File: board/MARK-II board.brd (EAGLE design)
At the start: 130 x 80 mm, 169 parts, among them IC1 MAX3243CPWR, IC10 IFX1963TBV, IC11 IFX1963TBV, IC12 ATTINY441-SSU, IC13 LD1117S33, IC2 FT230XS, IC3 ENC28J60SS, IC4 PCM5100, IC5 IS42S83200, IC6 MCP7940NSN, IC7 FM24CL16BG, IC8 AT25DN256SS, IC9 10M25SAE144, Q1 25MHz, Q2 32.768kHz, Q3 CMI-1275C-050, Q4 25MHz, Q5 18,432MHz, Q6 22.5792MHz, T1 BC337-16 A1, X1 MINI-USBUX60A-MB-5ST, X10 T821-106A1S100, X11 T821-110A1S100, X12 PJ-002BH-SMT-TR, X13 T821-106A1S100, X2 L717SDE09P1ACH4F, X3 L77HDE15SD1CH4R, X4 MD-60SM, X5 RB1-125BAG1A, X6 SJ1-3535NG, X7 MICROSD-HRS_DM3D, X8 BAT-HLD-002-SMT, X9 T821-120A1S100

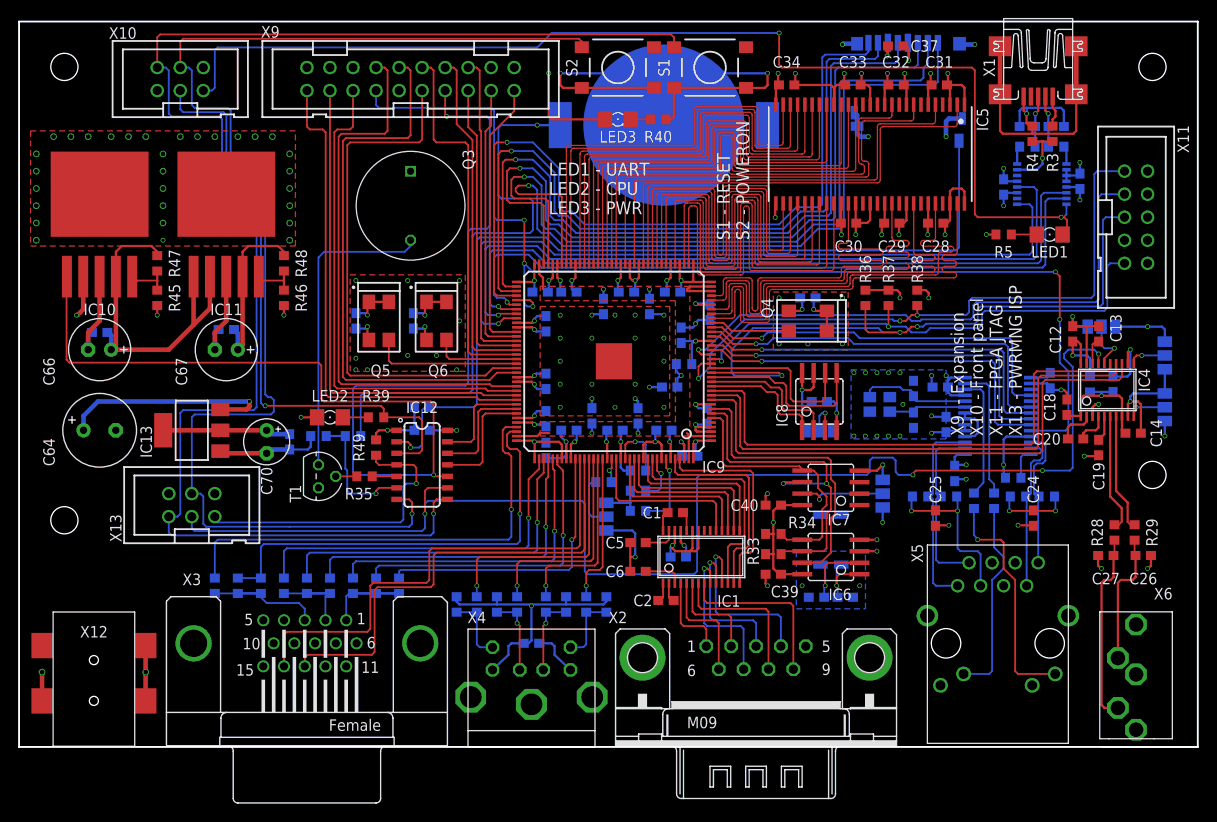
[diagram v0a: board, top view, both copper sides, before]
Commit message: power mng IC changet to Atmega48PB
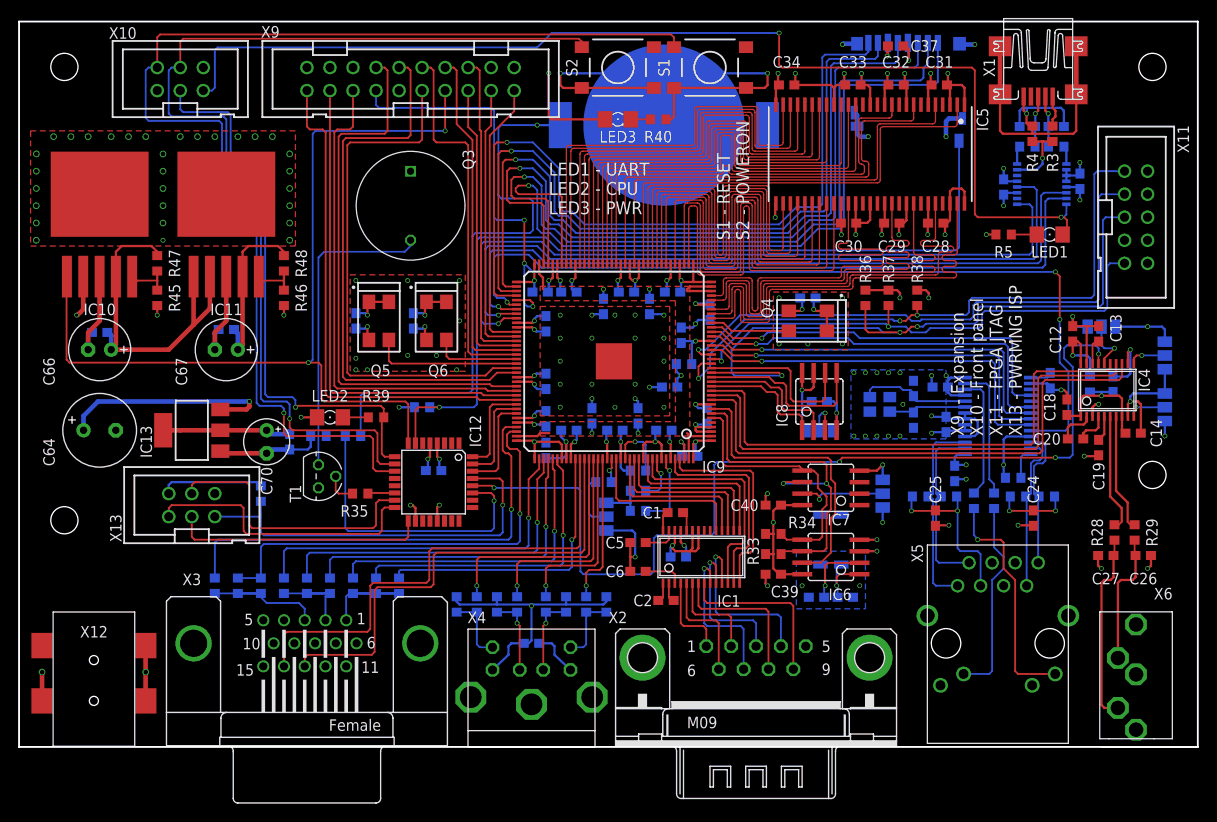
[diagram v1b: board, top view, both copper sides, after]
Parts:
- IC12: value ATTINY441-SSU -> ATMEGA48PB-AU; device ic:SO14 -> ic:TQFP32-08
- moved R49 13.7 mm to (26.7, 27.9), flipped to the bottom
- moved C65 4.62 mm to (45.7, 30.5), turned to 0 degrees
- moved IC12 2.84 mm to (45.7, 29.2)
- moved R35 1.96 mm to (37.6, 27.9)
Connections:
- removed net AUDIO_MUTE/ISP_SCK: IC12.9, IC4.17, X13.3
- removed net POWER_BTN/ISP_MOSI: IC12.7, S2.1, X10.4, X13.4
- removed net RESET_BTN/ISP_MISO: IC12.8, S1.1, X10.2, X13.1
- new net AUDIO_MUTE: IC12.28, IC4.17
- new net ISP_MISO: IC12.16, X13.1
- new net ISP_MOSI: IC12.15, X13.4
- new net ISP_SCK: IC12.17, X13.3
- new net POWER_BTN: IC12.10, S2.1, X10.4
- new net RESET_BTN: IC12.11, S1.1, X10.2
- net +3V3_SB: now also IC12.18, IC12.4; no longer IC12.1
- net CPU_LED: now also IC12.9; no longer IC12.3
- net GND: now also IC12.21, IC12.5; no longer IC12.14
- net ISP_RES: now also IC12.29; no longer IC12.4
- net N$21: now also IC12.27; no longer IC12.6
- net POWER_ON: now also IC12.8; no longer IC12.10
- net PWRMNG_RES: now also IC12.32; no longer IC12.13
- net PWRMNG_RX: now also IC12.30; no longer IC12.11
- net PWRMNG_TX: now also IC12.31; no longer IC12.12
- net SD_SW: now also IC12.7; no longer IC12.2
- net SPEAKER: now also IC12.14; no longer IC12.5
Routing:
- net RESET_BTN/ISP_MISO: track 166.6 -> 0.00 mm, vias 1 -> 0
- net AUDIO_MUTE/ISP_SCK: track 146.7 -> 0.00 mm, vias 4 -> 0
- net POWER_BTN/ISP_MOSI: track 144.6 -> 0.00 mm, vias 1 -> 0
- net RESET_BTN: track 0.00 -> 133.1 mm, vias 0 -> 1
- net POWER_BTN: track 0.00 -> 116.1 mm, vias 0 -> 1
- net AUDIO_MUTE: track 0.00 -> 105.4 mm, vias 0 -> 4
- net POWER_ON: track 133.3 -> 100.0 mm
- net ISP_MISO: track 0.00 -> 31.3 mm
- net ISP_MOSI: track 0.00 -> 30.9 mm
- net +3V3_SB: track 55.0 -> 83.9 mm, vias 1 -> 3
- net ISP_SCK: track 0.00 -> 28.1 mm
- net N$21: track 14.3 -> 35.0 mm
- net ISP_RES: track 33.8 -> 44.5 mm
- net CPU_LED: track 68.0 -> 63.1 mm
- net PWRMNG_RX: track 12.9 -> 10.8 mm
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
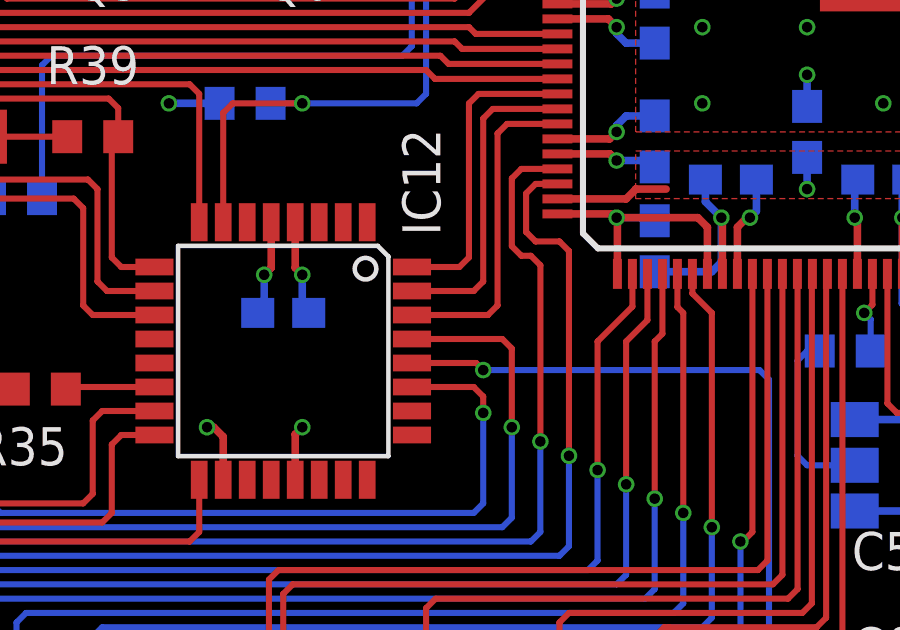
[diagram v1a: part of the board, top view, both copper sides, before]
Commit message: Small name changes to better suits HDL files
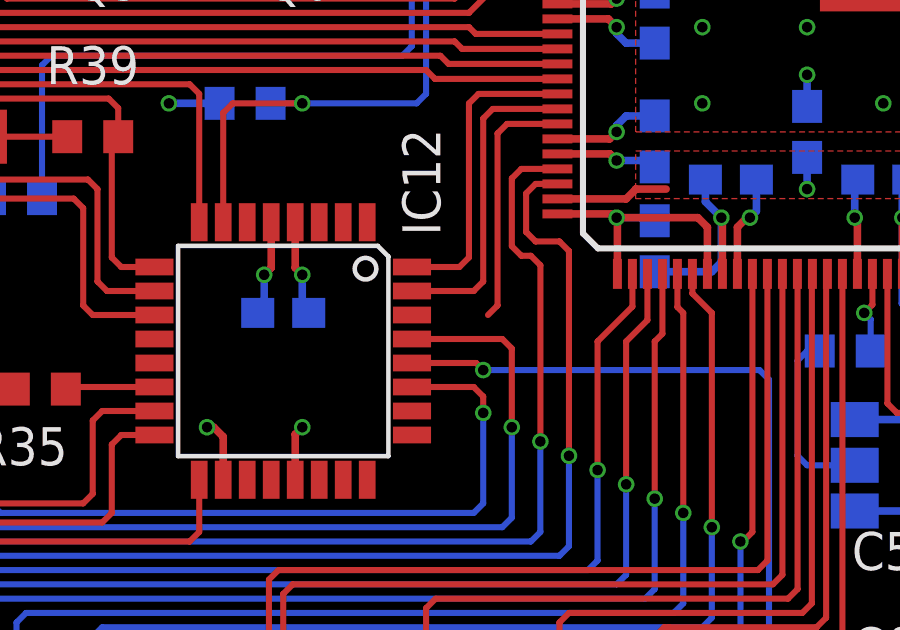
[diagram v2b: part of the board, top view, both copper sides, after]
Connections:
- net #RES renamed RES
- removed net EX_CMD4: IC9.87, X9.15
- removed net EX_DQ8: IC9.97, X9.5
- new net EX_CMD0: IC9.99, X9.1
- new net EX_DQ0: IC9.84, X9.19
- new net PWRMNG_RX00: IC9.102
- net EX_CMD1: now also IC9.98, X9.3; no longer IC9.99, X9.1
- net EX_CMD2: now also IC9.92, X9.11; no longer IC9.98, X9.3
- net EX_CMD3: now also IC9.87, X9.15; no longer IC9.92, X9.11
- net EX_DQ1: now also IC9.85, X9.17; no longer IC9.84, X9.19
- net EX_DQ2: now also IC9.86, X9.16; no longer IC9.85, X9.17
- net EX_DQ3: now also IC9.88, X9.14; no longer IC9.86, X9.16
- net EX_DQ4: now also IC9.89, X9.12; no longer IC9.88, X9.14
- net EX_DQ5: now also IC9.93, X9.10; no longer IC9.89, X9.12
- net EX_DQ6: now also IC9.96, X9.8; no longer IC9.93, X9.10
- net EX_DQ7: now also IC9.97, X9.5; no longer IC9.96, X9.8
- net PWRMNG_RX: now also IC12.31, IC9.101; no longer IC12.30, IC9.102
- net PWRMNG_TX: now also IC12.30; no longer IC12.31, IC9.101
- net UART0_RXD: now also IC2.1, IC9.81; no longer IC2.4, IC9.80
- net UART0_TXD: now also IC2.4, IC9.80; no longer IC2.1, IC9.81
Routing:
- net EX_CMD0: track 0.00 -> 56.5 mm
- net EX_DQ8: track 54.6 -> 0.00 mm
- net EX_CMD4: track 32.7 -> 0.00 mm
- net EX_DQ0: track 0.00 -> 30.5 mm
- net EX_CMD3: track 58.1 -> 32.7 mm
- net EX_DQ5: track 41.3 -> 61.9 mm
- net PWRMNG_TX: track 10.5 -> 0.00 mm
- net PWRMNG_RX00: track 0.00 -> 8.31 mm
- net EX_DQ7: track 60.6 -> 54.6 mm
- net EX_DQ2: track 30.6 -> 35.0 mm
- net EX_CMD2: track 53.8 -> 58.1 mm
- net EX_DQ4: track 37.6 -> 41.3 mm
- net EX_CMD1: track 56.5 -> 53.8 mm
- net EX_DQ3: track 35.0 -> 37.6 mm
- net EX_DQ6: track 61.9 -> 60.6 mm
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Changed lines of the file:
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@@
 <wire x1="109.5375" y1="44.7675" x2="109.5375" y2="39.105" width="0.2032" layer="16"/>
 </signal>
-<signal name="#RES" class="2">
+<signal name="RES" class="2">
 <contactref element="IC3" pad="10"/>
 <contactref element="IC9" pad="77"/>
@@
 <wire x1="112.87125" y1="64.29375" x2="112.87125" y2="64.92875" width="0.254" layer="16"/>
 </signal>
-<signal name="UART0_TXD" class="2">
+<signal name="UART0_RXD" class="2">
 <contactref element="IC2" pad="1"/>
 <contactref element="IC9" pad="81"/>
@@
 <wire x1="111.76" y1="54.61" x2="111.76" y2="59.53125" width="0.2032" layer="16"/>
 </signal>
-<signal name="UART0_RXD" class="2">
+<signal name="UART0_TXD" class="2">
 <contactref element="IC2" pad="4"/>
 <contactref element="IC9" pad="80"/>
@@
 <wire x1="69.6775" y1="29.05125" x2="79.155" y2="29.05125" width="0.2032" layer="1"/>
 </signal>
-<signal name="EX_DQ1" class="2">
+<signal name="EX_DQ0" class="2">
 <contactref element="IC9" pad="84"/>
 <wire x1="54.86" y1="45.78" x2="52.22875" y2="45.78" width="0.2032" layer="1"/>
@@
 <wire x1="54.61" y1="70.12305" x2="54.61" y2="72.39" width="0.2032" layer="1"/>
 </signal>
-<signal name="EX_DQ2" class="2">
+<signal name="EX_DQ1" class="2">
 <contactref element="IC9" pad="85"/>
 <wire x1="54.86" y1="45.28" x2="51.7525" y2="45.28" width="0.2032" layer="1"/>
@@
 <wire x1="52.07" y1="68.53555" x2="52.07" y2="72.39" width="0.2032" layer="1"/>
 </signal>
-<signal name="EX_DQ4" class="2">
+<signal name="EX_DQ3" class="2">
 <contactref element="IC9" pad="88"/>
 <wire x1="54.86" y1="43.78" x2="50.32375" y2="43.78" width="0.2032" layer="1"/>
@@
 <wire x1="46.99" y1="74.93" x2="47.9425" y2="74.93" width="0.2032" layer="1"/>
 </signal>
-<signal name="EX_DQ5" class="2">
+<signal name="EX_DQ4" class="2">
 <contactref element="IC9" pad="89"/>
 <wire x1="45.4025" y1="74.93" x2="45.72" y2="74.6125" width="0.2032" layer="1"/>
@@
 <wire x1="44.45" y1="74.93" x2="45.4025" y2="74.93" width="0.2032" layer="1"/>
 </signal>
-<signal name="EX_DQ6" class="2">
+<signal name="EX_DQ5" class="2">
 <contactref element="IC9" pad="93"/>
 <wire x1="42.8625" y1="74.93" x2="43.18" y2="74.6125" width="0.2032" layer="1"/>
@@
 <wire x1="41.91" y1="74.93" x2="42.8625" y2="74.93" width="0.2032" layer="1"/>
 </signal>
-<signal name="EX_DQ7" class="2">
+<signal name="EX_DQ6" class="2">
 <contactref element="IC9" pad="96"/>
 <wire x1="40.3225" y1="74.93" x2="40.64" y2="74.6125" width="0.2032" layer="1"/>
@@
 <wire x1="39.37" y1="74.93" x2="40.3225" y2="74.93" width="0.2032" layer="1"/>
 </signal>
-<signal name="EX_DQ8" class="2">
+<signal name="EX_DQ7" class="2">
 <contactref element="IC9" pad="97"/>
 <wire x1="36.5125" y1="68.10375" x2="36.83" y2="68.42125" width="0.2032" layer="1"/>
@@
 <wire x1="36.83" y1="68.42125" x2="36.83" y2="72.39" width="0.2032" layer="1"/>
 </signal>
-<signal name="EX_DQ3" class="2">
+<signal name="EX_DQ2" class="2">
 <contactref element="IC9" pad="86"/>
 <wire x1="54.86" y1="44.78" x2="51.27625" y2="44.78" width="0.2032" layer="1"/>
@@
 <wire x1="49.53" y1="74.93" x2="50.4825" y2="74.93" width="0.2032" layer="1"/>
 </signal>
-<signal name="EX_CMD1" class="2">
+<signal name="EX_CMD0" class="2">
 <contactref element="IC9" pad="99"/>
 <wire x1="33.81375" y1="38.89375" x2="34.13125" y2="38.57625" width="0.2032" layer="1"/>
@@
 <wire x1="31.75" y1="68.42125" x2="31.75" y2="72.39" width="0.2032" layer="1"/>
 </signal>
-<signal name="EX_CMD2" class="2">
+<signal name="EX_CMD1" class="2">
 <contactref element="IC9" pad="98"/>
 <wire x1="34.29" y1="39.37" x2="34.6075" y2="39.0525" width="0.2032" layer="1"/>
@@
 <wire x1="34.29" y1="72.39" x2="34.29" y2="39.37" width="0.2032" layer="1"/>
 </signal>
-<signal name="EX_CMD4" class="2">
+<signal name="EX_CMD3" class="2">
 <contactref element="IC9" pad="87"/>
 <wire x1="54.86" y1="44.28" x2="50.8" y2="44.28" width="0.2032" layer="1"/>
@@
 <wire x1="49.53" y1="68.3768" x2="49.53" y2="72.39" width="0.2032" layer="1"/>
 </signal>
-<signal name="EX_CMD3" class="2">
+<signal name="EX_CMD2" class="2">
 <contactref element="IC9" pad="92"/>
 <wire x1="44.1325" y1="66.675" x2="44.45" y2="66.9925" width="0.2032" layer="1"/>
@@
 <wire x1="52.86375" y1="60.80125" x2="52.86375" y2="68.2625" width="0.2032" layer="16"/>
 </signal>
-<signal name="PWRMNG_TX" class="2">
+<signal name="PWRMNG_RX" class="2">
 <contactref element="IC9" pad="101"/>
 <contactref element="IC12" pad="31"/>
@@
 <wire x1="52.3875" y1="36.9625" x2="52.3875" y2="31.5275" width="0.2032" layer="1"/>
 </signal>
-<signal name="PWRMNG_RX" class="2">
+<signal name="PWRMNG_RX00" class="2">
 <contactref element="IC9" pad="102"/>
-<contactref element="IC12" pad="30"/>
 <wire x1="54.86" y1="36.78" x2="53.18125" y2="36.78" width="0.2032" layer="1"/>
 <wire x1="53.18125" y1="36.78" x2="52.86375" y2="36.4625" width="0.2032" layer="1"/>
 <wire x1="52.86375" y1="30.7275" x2="52.54625" y2="30.41" width="0.2032" layer="1"/>
-<wire x1="52.54625" y1="30.41" x2="50.0126" y2="30.41" width="0.2032" layer="1"/>
 <wire x1="52.86375" y1="36.4625" x2="52.86375" y2="30.7275" width="0.2032" layer="1"/>
 </signal>
@@
 <wire x1="19.3675" y1="22.86" x2="42.6025" y2="22.86" width="0.2032" layer="1"/>
 </signal>
+<signal name="PWRMNG_TX" class="2">
+<contactref element="IC12" pad="30"/>
+</signal>
 </signals>

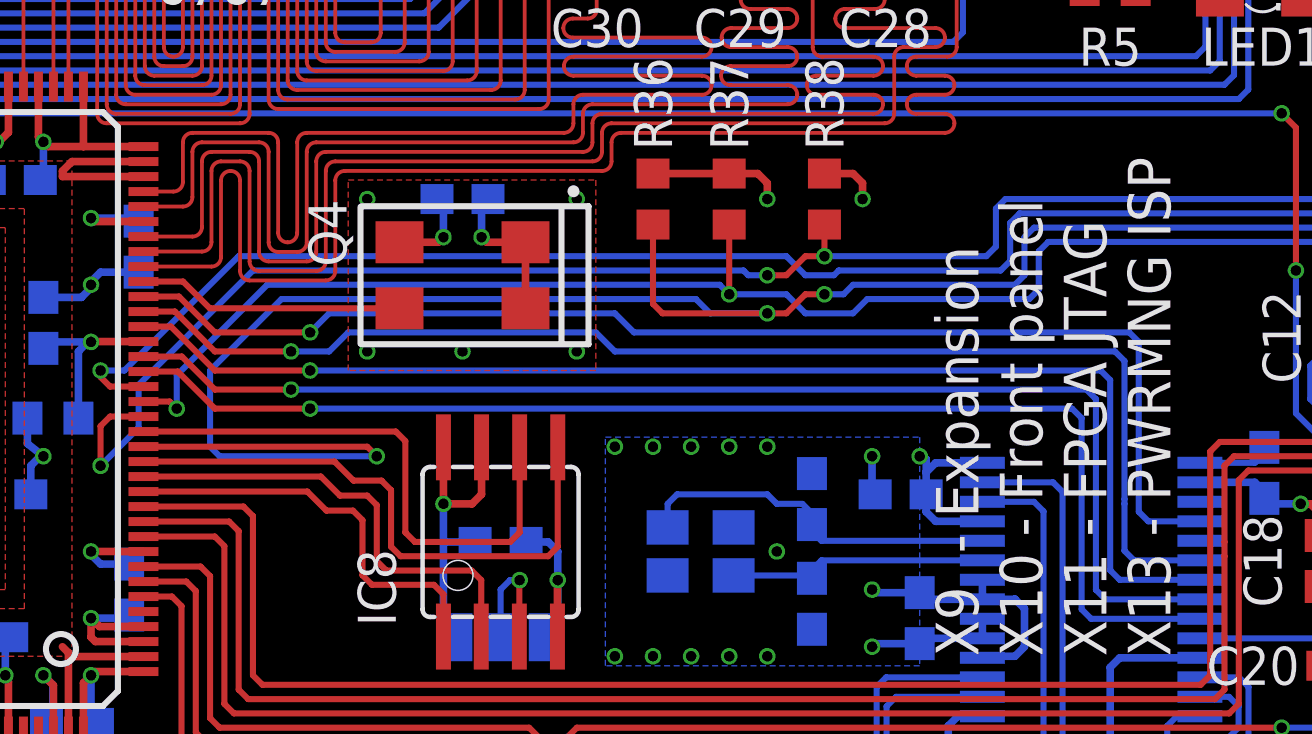
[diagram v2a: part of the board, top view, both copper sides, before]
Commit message: Fix clk for pll
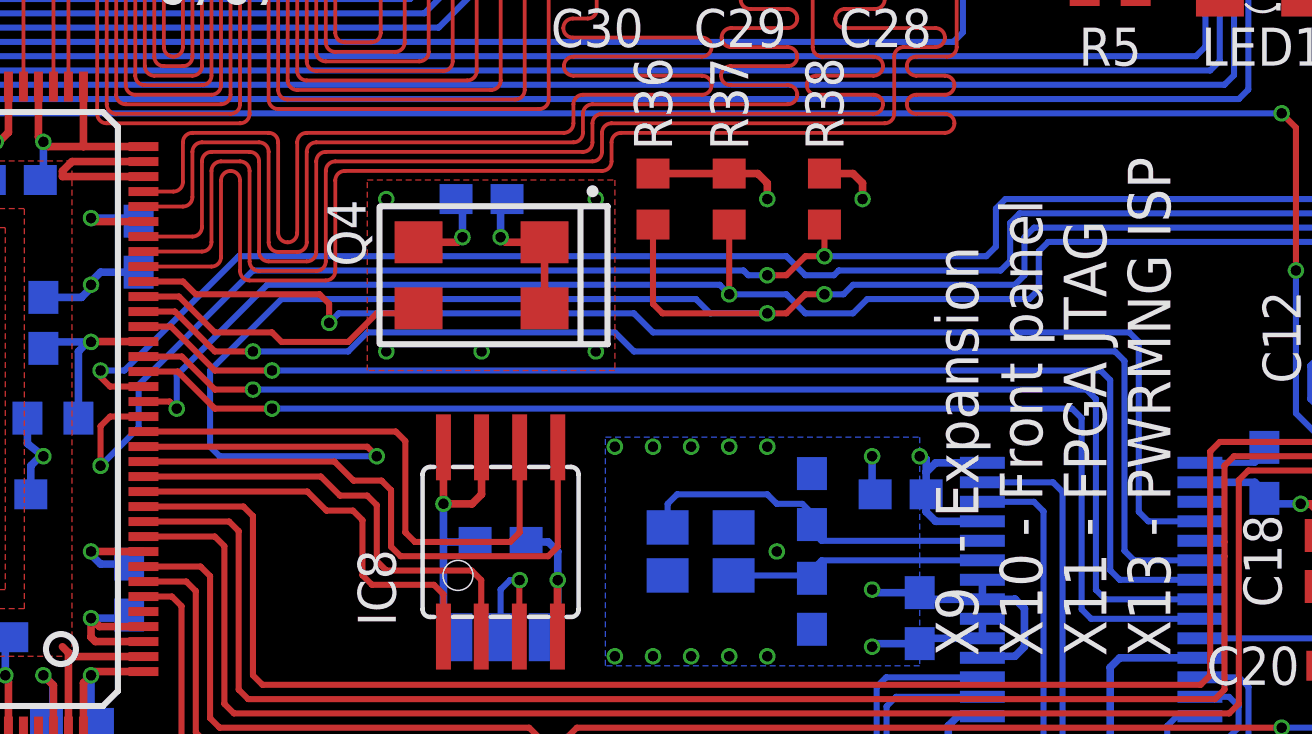
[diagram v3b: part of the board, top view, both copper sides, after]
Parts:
- moved C41 0.63 mm to (87.6, 49.5)
- moved Q4 0.63 mm to (87.6, 47.0)
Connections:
- net CLK_25M: now also IC9.26; no longer IC9.27
- net ENC_INT: now also IC9.27; no longer IC9.26
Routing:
- net CLK_25M: track 8.90 -> 10.3 mm

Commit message: Fixed pwrmng uart connection
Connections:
- net FLASH_#CS renamed FLASH_CS
- removed net PWRMNG_RX00: IC9.102
- net PWRMNG_TX: now also IC9.102
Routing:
- net PWRMNG_TX: track 0.00 -> 10.8 mm
- net PWRMNG_RX00: track 8.31 -> 0.00 mm
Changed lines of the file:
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@@
 <wire x1="78.89875" y1="31.90875" x2="78.58125" y2="32.22625" width="0.2032" layer="1"/>
 </signal>
-<signal name="FLASH_#CS" class="2">
+<signal name="FLASH_CS" class="2">
 <contactref element="IC8" pad="1"/>
 <contactref element="IC9" pad="13"/>
@@
 <wire x1="52.07" y1="31.21" x2="50.0126" y2="31.21" width="0.2032" layer="1"/>
 <wire x1="52.3875" y1="36.9625" x2="52.3875" y2="31.5275" width="0.2032" layer="1"/>
-</signal>
-<signal name="PWRMNG_RX00" class="2">
-<contactref element="IC9" pad="102"/>
-<wire x1="54.86" y1="36.78" x2="53.18125" y2="36.78" width="0.2032" layer="1"/>
-<wire x1="53.18125" y1="36.78" x2="52.86375" y2="36.4625" width="0.2032" layer="1"/>
-<wire x1="52.86375" y1="30.7275" x2="52.54625" y2="30.41" width="0.2032" layer="1"/>
-<wire x1="52.86375" y1="36.4625" x2="52.86375" y2="30.7275" width="0.2032" layer="1"/>
 </signal>
 <signal name="PWRMNG_RES" class="2">
@@
 <signal name="PWRMNG_TX" class="2">
 <contactref element="IC12" pad="30"/>
+<contactref element="IC9" pad="102"/>
+<wire x1="54.86" y1="36.78" x2="53.18125" y2="36.78" width="0.2032" layer="1"/>
+<wire x1="53.18125" y1="36.78" x2="52.86375" y2="36.4625" width="0.2032" layer="1"/>
+<wire x1="52.54625" y1="30.41" x2="52.86375" y2="30.7275" width="0.2032" layer="1"/>
+<wire x1="52.86375" y1="36.4625" x2="52.86375" y2="30.7275" width="0.2032" layer="1"/>
+<wire x1="50.0126" y1="30.41" x2="52.54625" y2="30.41" width="0.2032" layer="1"/>
 </signal>
 </signals>
